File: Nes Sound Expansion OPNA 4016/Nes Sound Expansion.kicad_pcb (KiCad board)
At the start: 2 copper layers, 86.4 x 87.6 mm, 41 parts, among them J1 NES-SNES Port1, J2 NES-SNES Port2, J3 EXP 1-24, J4 EXP 25-48, J5 EN Switch, J6 AudioJack2_Ground_Switch, J7 EN LED, U1 74LS139, U10 74LS257, U2 74LS132, U6 74LS174, U7 74LS174, U8 74LS257, U9 74LS257, X1 CXO_DIP8

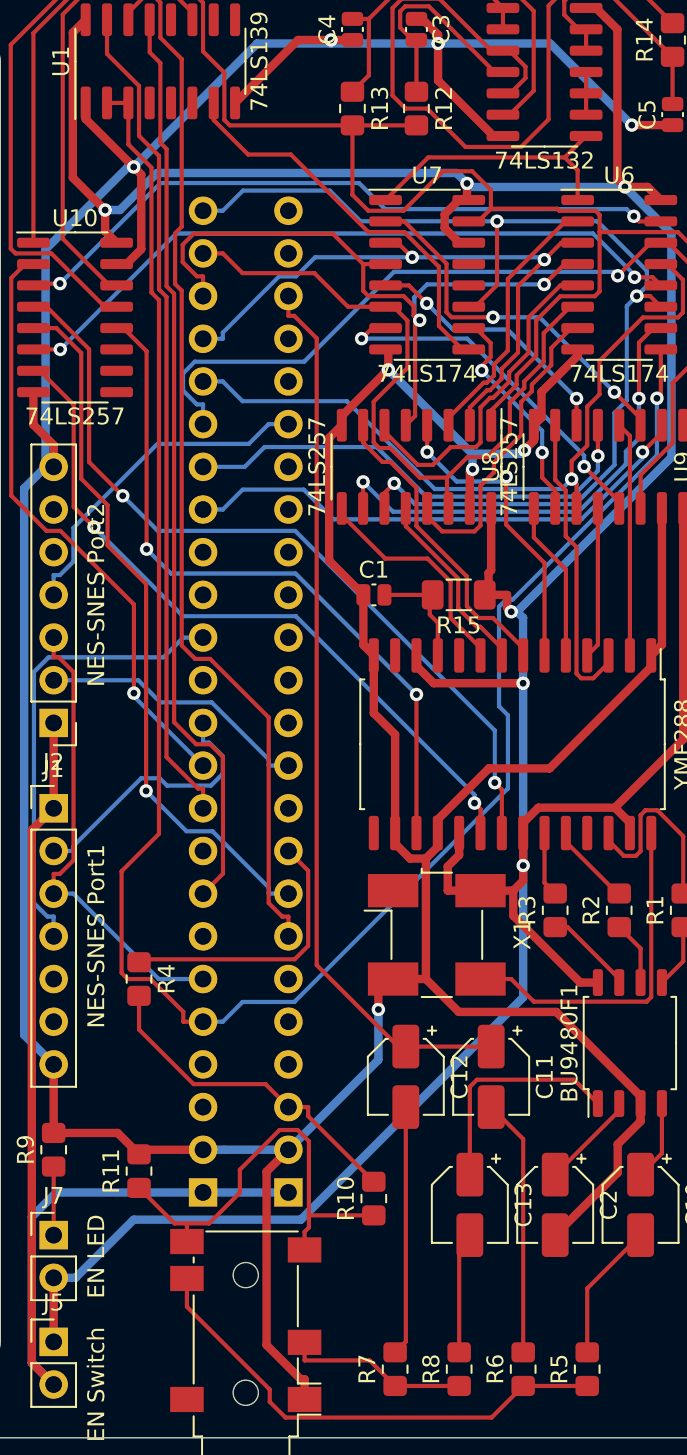
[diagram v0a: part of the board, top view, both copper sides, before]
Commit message: Fixed floating signals and famicom exp audio
Addressing issues caused by floating signals when a cart without hardware addressing is used
Added famicom expansion resistors to all 3 popular EXP pins.
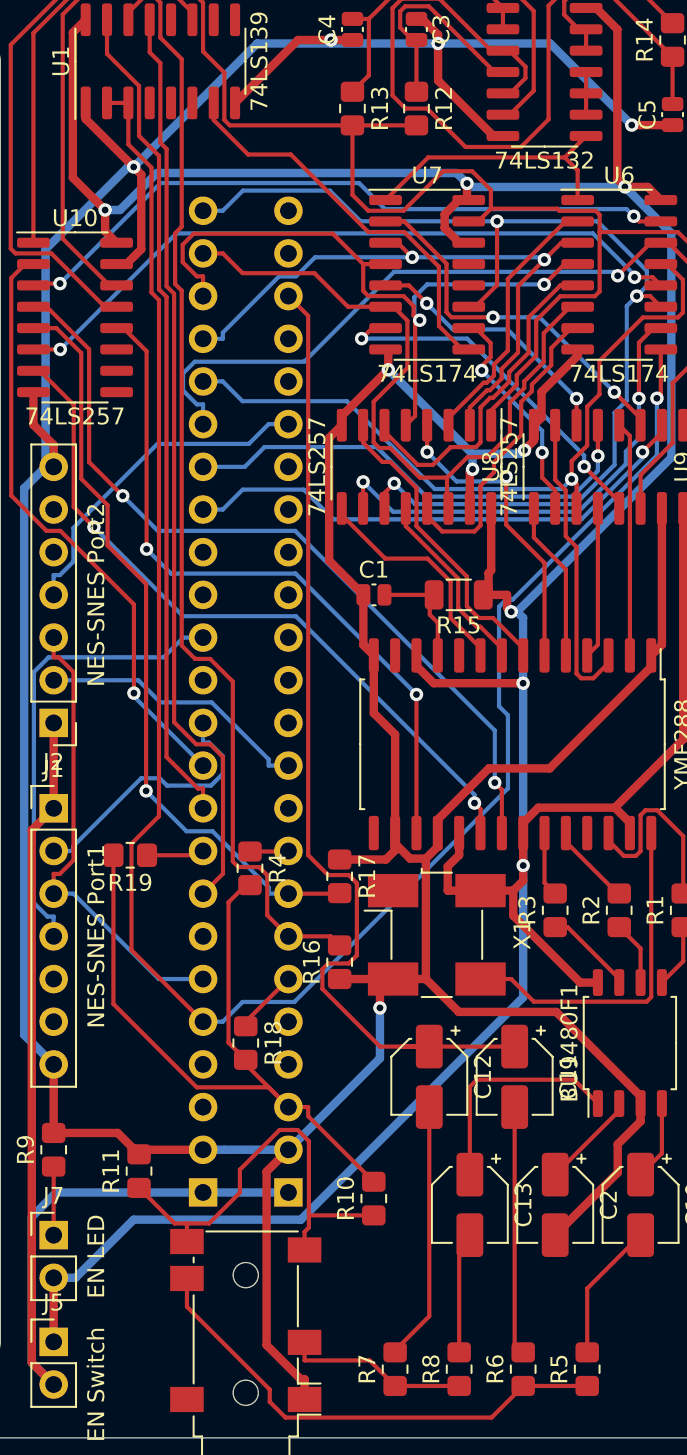
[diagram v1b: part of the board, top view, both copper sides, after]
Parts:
- added R16: 1k, Resistor_SMD:R_0805_2012Metric_Pad1.20x1.40mm_HandSolder, F.Cu at (116.1, 95.5)
- added R17: 1k, Resistor_SMD:R_0805_2012Metric_Pad1.20x1.40mm_HandSolder, F.Cu at (116.1, 90.4)
- added R18: 47k, Resistor_SMD:R_0805_2012Metric_Pad1.20x1.40mm_HandSolder, F.Cu at (110.5, 100.3)
- added R19: 47k, Resistor_SMD:R_0805_2012Metric_Pad1.20x1.40mm_HandSolder, F.Cu at (103.6, 89.2)
- R15: footprint Resistor_SMD:R_1206_3216Metric_Pad1.30x1.75mm_HandSolder -> Resistor_SMD:R_1206_3216Metric
- R5, R8: value 1k -> 600Ω
- R6, R7: value 1k -> 3k
- moved R4 9.33 mm to (110.7, 89.9)
- moved C11 1.40 mm to (126.5, 102.3)
- moved C12 1.40 mm to (121.4, 102.3)
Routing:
- net AudIn: track 20.0 -> 44.2 mm
- net Net-(J3-Pad9): track 16.6 -> 2.55 mm
- net GND: track 297.3 -> 305.1 mm
- net Aud: track 53.1 -> 59.7 mm
- net Net-(J3-Pad6): track 0.00 -> 3.86 mm
- net A14: track 62.6 -> 66.4 mm
- net Net-(J4-Pad9): track 0.00 -> 3.44 mm
- net A13: track 42.3 -> 45.4 mm
- net OUT1: track 115.6 -> 113.6 mm
- net Net-(C12-Pad2): track 14.9 -> 15.4 mm
- net Net-(C11-Pad2): track 15.4 -> 14.8 mm

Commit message: minor update
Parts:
- moved R17 9.72 mm to (117.1, 100.1), turned to 180 degrees
- moved R16 7.92 mm to (117.1, 103.4), turned to 180 degrees
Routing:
- net A14: track 66.4 -> 74.2 mm
- net A13: track 45.4 -> 52.2 mm
- net Aud: track 59.7 -> 63.3 mm
- net GND: track 305.1 -> 302.6 mm
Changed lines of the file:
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@@
   )
   (module Resistor_SMD:R_0805_2012Metric_Pad1.20x1.40mm_HandSolder (layer F.Cu)
-    (at 116.078 90.408 270)
+    (at 117.094 100.076 180)
     (descr "Resistor SMD 0805 (2012 Metric), square (rectangular) end terminal, IPC_7351 nominal with elongated pad for handsoldering. (Body size source: IPC-SM-782 page 72, https://www.pcb-3d.com/wordpress/wp-content/uploads/ipc-sm-782a_amendment_1_and_2.pdf), generated with kicad-footprint-generator")
     (tags "resistor handsolder")
     (attr smd)
-    (fp_text reference R17 (at 0 -1.65 90) (layer F.SilkS)
-      (effects (font (size 1 1) (thickness 0.15)))
-    )
-    (fp_text value 1k (at 0 1.65 90) (layer F.Fab)
-      (effects (font (size 1 1) (thickness 0.15)))
-    )
-    (fp_text user %R (at 0 0 90) (layer F.Fab)
+    (fp_text reference R17 (at 0 -1.65) (layer F.SilkS)
+      (effects (font (size 1 1) (thickness 0.15)))
+    )
+    (fp_text value 1k (at 0 1.65) (layer F.Fab)
+      (effects (font (size 1 1) (thickness 0.15)))
+    )
+    (fp_text user %R (at 0 0) (layer F.Fab)
       (effects (font (size 0.5 0.5) (thickness 0.08)))
     )
@@
     (fp_line (start 1.85 -0.95) (end 1.85 0.95) (layer F.CrtYd) (width 0.05))
     (fp_line (start 1.85 0.95) (end -1.85 0.95) (layer F.CrtYd) (width 0.05))
-    (pad 2 smd roundrect (at 1 0 270) (size 1.2 1.4) (layers F.Cu F.Paste F.Mask) (roundrect_rratio 0.208333)
+    (pad 2 smd roundrect (at 1 0 180) (size 1.2 1.4) (layers F.Cu F.Paste F.Mask) (roundrect_rratio 0.208333)
       (net 88 A13))
-    (pad 1 smd roundrect (at -1 0 270) (size 1.2 1.4) (layers F.Cu F.Paste F.Mask) (roundrect_rratio 0.208333)
+    (pad 1 smd roundrect (at -1 0 180) (size 1.2 1.4) (layers F.Cu F.Paste F.Mask) (roundrect_rratio 0.208333)
       (net 3 GND))
     (model ${KISYS3DMOD}/Resistor_SMD.3dshapes/R_0805_2012Metric.wrl
@@
   )
   (module Resistor_SMD:R_0805_2012Metric_Pad1.20x1.40mm_HandSolder (layer F.Cu)
-    (at 116.078 95.52 90)
+    (at 117.094 103.378 180)
     (descr "Resistor SMD 0805 (2012 Metric), square (rectangular) end terminal, IPC_7351 nominal with elongated pad for handsoldering. (Body size source: IPC-SM-782 page 72, https://www.pcb-3d.com/wordpress/wp-content/uploads/ipc-sm-782a_amendment_1_and_2.pdf), generated with kicad-footprint-generator")
     (tags "resistor handsolder")
     (attr smd)
-    (fp_text reference R16 (at 0 -1.65 90) (layer F.SilkS)
-      (effects (font (size 1 1) (thickness 0.15)))
-    )
-    (fp_text value 1k (at 0 1.65 90) (layer F.Fab)
-      (effects (font (size 1 1) (thickness 0.15)))
-    )
-    (fp_text user %R (at 0 0 90) (layer F.Fab)
+    (fp_text reference R16 (at 0 -1.65) (layer F.SilkS)
+      (effects (font (size 1 1) (thickness 0.15)))
+    )
+    (fp_text value 1k (at 0 1.65) (layer F.Fab)
+      (effects (font (size 1 1) (thickness 0.15)))
+    )
+    (fp_text user %R (at 0 0) (layer F.Fab)
       (effects (font (size 0.5 0.5) (thickness 0.08)))
     )
@@
     (fp_line (start 1.85 -0.95) (end 1.85 0.95) (layer F.CrtYd) (width 0.05))
     (fp_line (start 1.85 0.95) (end -1.85 0.95) (layer F.CrtYd) (width 0.05))
-    (pad 2 smd roundrect (at 1 0 90) (size 1.2 1.4) (layers F.Cu F.Paste F.Mask) (roundrect_rratio 0.208333)
+    (pad 2 smd roundrect (at 1 0 180) (size 1.2 1.4) (layers F.Cu F.Paste F.Mask) (roundrect_rratio 0.208333)
       (net 102 A14))
-    (pad 1 smd roundrect (at -1 0 90) (size 1.2 1.4) (layers F.Cu F.Paste F.Mask) (roundrect_rratio 0.208333)
+    (pad 1 smd roundrect (at -1 0 180) (size 1.2 1.4) (layers F.Cu F.Paste F.Mask) (roundrect_rratio 0.208333)
       (net 3 GND))
     (model ${KISYS3DMOD}/Resistor_SMD.3dshapes/R_0805_2012Metric.wrl
@@
   (segment (start 121.9366 40.3362) (end 120.9854 39.385) (width 0.5) (layer F.Cu) (net 3))
   (segment (start 120.9854 39.385) (end 120.65 39.385) (width 0.5) (layer F.Cu) (net 3))
-  (segment (start 118.11 77.265) (end 117.4905 76.6455) (width 0.5) (layer F.Cu) (net 3))
-  (segment (start 117.4905 76.6455) (end 117.4905 73.66) (width 0.5) (layer F.Cu) (net 3))
   (segment (start 99.06 66.04) (end 99.06 64.7397) (width 0.5) (layer F.Cu) (net 3))
   (segment (start 99.06 64.7397) (end 97.855 63.5347) (width 0.5) (layer F.Cu) (net 3))
@@
   (segment (start 118.477015 97.302985) (end 118.477015 98.236885) (width 0.5) (layer F.Cu) (net 3))
   (segment (start 113.03 106.68) (end 118.477015 101.232985) (width 0.5) (layer B.Cu) (net 3))
-  (segment (start 119.38 88.86) (end 119.38 87.835) (width 0.5) (layer F.Cu) (net 3))
-  (segment (start 118.832 89.408) (end 119.38 88.86) (width 0.5) (layer F.Cu) (net 3))
-  (segment (start 116.078 89.408) (end 118.832 89.408) (width 0.5) (layer F.Cu) (net 3))
-  (segment (start 116.078 96.52) (end 119.26 96.52) (width 0.5) (layer F.Cu) (net 3))
+  (segment (start 118.477015 99.692985) (end 118.094 100.076) (width 0.5) (layer F.Cu) (net 3))
+  (segment (start 118.477015 98.236885) (end 118.477015 99.692985) (width 0.5) (layer F.Cu) (net 3))
+  (segment (start 118.094 100.076) (end 118.094 103.378) (width 0.5) (layer F.Cu) (net 3))
+  (segment (start 117.4905 74.241666) (end 117.4905 73.66) (width 0.5) (layer F.Cu) (net 3))
+  (segment (start 118.11 77.265) (end 118.11 74.861166) (width 0.5) (layer F.Cu) (net 3))
+  (segment (start 118.11 74.861166) (end 117.4905 74.241666) (width 0.5) (layer F.Cu) (net 3))
   (segment (start 133.985 111.76) (end 130.81 114.935) (width 0.25) (layer F.Cu) (net 4))
   (segment (start 130.81 114.935) (end 130.81 118.735) (width 0.25) (layer F.Cu) (net 4))
@@
   (segment (start 113.03 91.44) (end 111.8547 91.44) (width 0.25) (layer B.Cu) (net 88))
   (via (at 104.5605 85.3257) (size 0.8) (layers F.Cu B.Cu) (net 88))
-  (segment (start 116.046 91.44) (end 116.078 91.408) (width 0.25) (layer F.Cu) (net 88))
-  (segment (start 113.03 91.44) (end 116.046 91.44) (width 0.25) (layer F.Cu) (net 88))
+  (segment (start 116.094 94.504) (end 113.03 91.44) (width 0.25) (layer F.Cu) (net 88))
+  (segment (start 116.094 100.076) (end 116.094 94.504) (width 0.25) (layer F.Cu) (net 88))
   (segment (start 103.8352 79.5082) (end 103.8352 74.2246) (width 0.25) (layer F.Cu) (net 89))
   (segment (start 103.8352 74.2246) (end 99.4606 69.85) (width 0.25) (layer F.Cu) (net 89))
@@
   (segment (start 126.492 100.54) (end 121.412 100.54) (width 0.25) (layer F.Cu) (net 96))
   (segment (start 119.75481 100.54) (end 121.412 100.54) (width 0.25) (layer F.Cu) (net 96))
-  (segment (start 113.03 55.88) (end 114.205001 57.055001) (width 0.25) (layer F.Cu) (net 96))
-  (segment (start 115.38982 90.33301) (end 114.205001 89.148191) (width 0.25) (layer F.Cu) (net 96))
-  (segment (start 116.6162 90.33301) (end 115.38982 90.33301) (width 0.25) (layer F.Cu) (net 96))
-  (segment (start 114.205001 89.148191) (end 114.205001 57.055001) (width 0.25) (layer F.Cu) (net 96))
-  (segment (start 116.6162 95.59499) (end 117.10301 95.10818) (width 0.25) (layer F.Cu) (net 96))
-  (segment (start 117.10301 90.81982) (end 116.6162 90.33301) (width 0.25) (layer F.Cu) (net 96))
-  (segment (start 115.38982 95.59499) (end 116.6162 95.59499) (width 0.25) (layer F.Cu) (net 96))
-  (segment (start 117.10301 95.10818) (end 117.10301 90.81982) (width 0.25) (layer F.Cu) (net 96))
-  (segment (start 115.05299 95.93182) (end 115.38982 95.59499) (width 0.25) (layer F.Cu) (net 96))
-  (segment (start 115.05299 97.10818) (end 115.05299 95.93182) (width 0.25) (layer F.Cu) (net 96))
-  (segment (start 118.48481 100.54) (end 115.05299 97.10818) (width 0.25) (layer F.Cu) (net 96))
-  (segment (start 121.412 100.54) (end 118.48481 100.54) (width 0.25) (layer F.Cu) (net 96))
+  (segment (start 114.205001 57.055001) (end 114.046 56.896) (width 0.25) (layer F.Cu) (net 96))
+  (segment (start 114.205001 71.769355) (end 114.205001 57.055001) (width 0.25) (layer F.Cu) (net 96))
+  (segment (start 117.01901 74.583364) (end 114.205001 71.769355) (width 0.25) (layer F.Cu) (net 96))
+  (segment (start 117.01901 103.9162) (end 117.01901 74.583364) (width 0.25) (layer F.Cu) (net 96))
+  (segment (start 117.50582 104.40301) (end 117.01901 103.9162) (width 0.25) (layer F.Cu) (net 96))
+  (segment (start 120.28699 102.7982) (end 118.68218 104.40301) (width 0.25) (layer F.Cu) (net 96))
+  (segment (start 113.03 55.88) (end 114.046 56.896) (width 0.25) (layer F.Cu) (net 96))
+  (segment (start 118.68218 104.40301) (end 117.50582 104.40301) (width 0.25) (layer F.Cu) (net 96))
+  (segment (start 121.412 100.54) (end 120.28699 101.66501) (width 0.25) (layer F.Cu) (net 96))
+  (segment (start 120.28699 101.66501) (end 120.28699 102.7982) (width 0.25) (layer F.Cu) (net 96))
   (segment (start 106.7747 76.2) (end 105.5994 77.3753) (width 0.25) (layer B.Cu) (net 97))
   (segment (start 105.5994 77.3753) (end 98.7587 77.3753) (width 0.25) (layer B.Cu) (net 97))
@@
   (segment (start 110.05582 89.85701) (end 109.71899 89.52018) (width 0.25) (layer F.Cu) (net 102))
   (segment (start 113.03 93.98) (end 111.76901 92.71901) (width 0.25) (layer F.Cu) (net 102))
-  (segment (start 115.538 93.98) (end 116.078 94.52) (width 0.25) (layer F.Cu) (net 102))
-  (segment (start 113.03 93.98) (end 115.538 93.98) (width 0.25) (layer F.Cu) (net 102))
+  (segment (start 114.205001 95.155001) (end 113.03 93.98) (width 0.25) (layer F.Cu) (net 102))
+  (segment (start 114.205001 102.089001) (end 114.205001 95.155001) (width 0.25) (layer F.Cu) (net 102))
+  (segment (start 115.494 103.378) (end 114.205001 102.089001) (width 0.25) (layer F.Cu) (net 102))
+  (segment (start 116.094 103.378) (end 115.494 103.378) (width 0.25) (layer F.Cu) (net 102))
   (segment (start 107.95 85.1847) (end 107.6495 85.1847) (width 0.25) (layer F.Cu) (net 103))
   (segment (start 107.6495 85.1847) (end 105.7764 83.3116) (width 0.25) (layer F.Cu) (net 103))

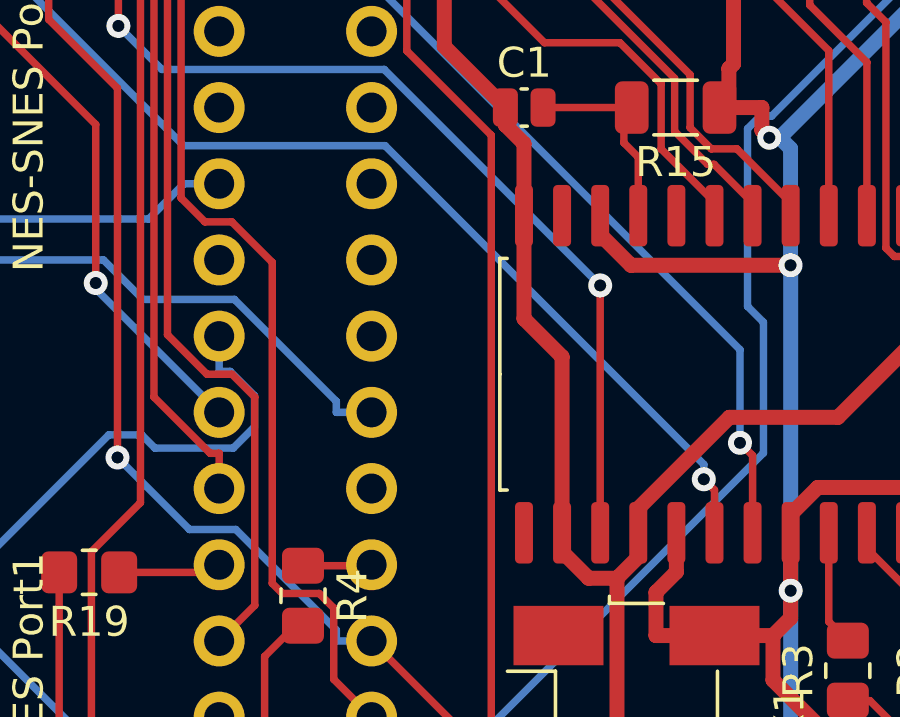
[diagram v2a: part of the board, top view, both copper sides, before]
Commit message: Added IRQ from the YMF288
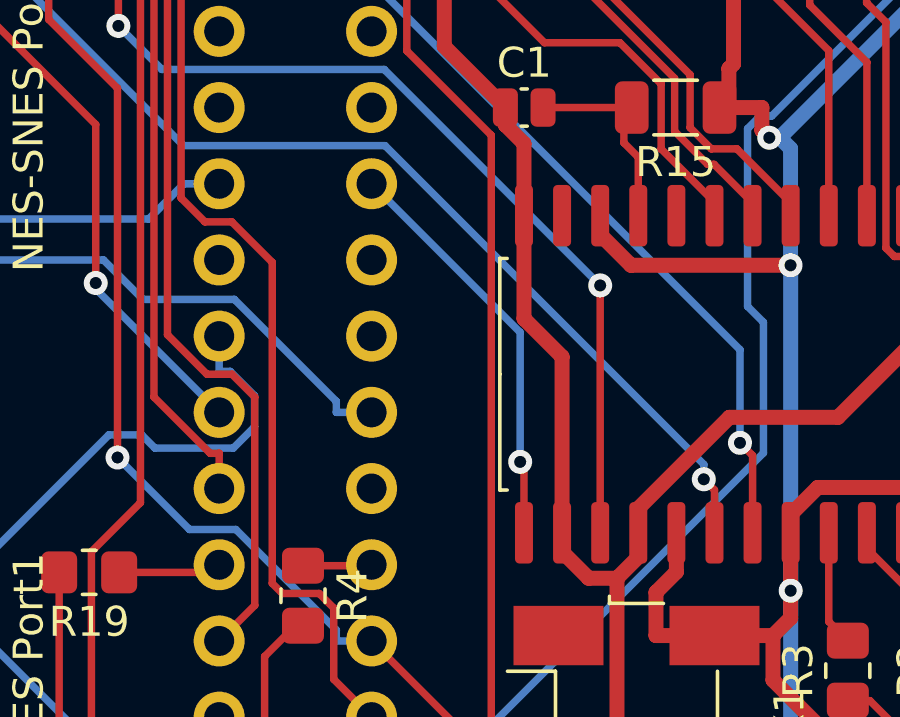
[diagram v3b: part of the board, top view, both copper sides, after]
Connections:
- net Net-(J3-Pad4) renamed NMI
- J3 pad 14: Net-(J3-Pad14) -> IRQ
- YMF288 pad 15: Net-(YMF288-Pad15) -> IRQ
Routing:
- net IRQ: track 0.00 -> 13.7 mm, vias 0 -> 1
